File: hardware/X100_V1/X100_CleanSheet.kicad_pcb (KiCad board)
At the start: 4 copper layers, 45 x 45 mm, 205 parts, among them J401 124019772112A, J501 1040310811, J601 SM04B-GHS-TB(LF)(SN), J701 SM06B-GHS-TB(LF)(SN), J702 SM06B-GHS-TB(LF)(SN), J703 SM06B-GHS-TB(LF)(SN), J704 SM04B-GHS-TB(LF)(SN), J801 OUT1 /GND, J802 OUT2 /GND, J803 OUT3 /GND, J804 OUT4 /GND, J805 OUT5 /GND, J806 OUT6 /GND, J807 SWD:1REF2GND3IO4CLK5NRST, J808 BATTERY/bench3S-6S ONLY, J809 CURRENT monitor only, Q101 DMP6023LSS-13, U101 TPS54360BDDAR, U102 AP63203WU-7, U103 TPS7A2033PDBVR, U104 TPS2553DBVR, U201 STM32H743VIT6, U301 BMI088, U302 SPL06-001, U401 TPD2E2U06QDBZRQ1, U402 SN74LVC1G17DBVR, U403 TPD2E2U06QDBZRQ1, U404 TPD2E2U06QDBZRQ1, U601 TCAN3414DR, U801 TMUX1511PWR, Y201 8.000MHz /CL20pF

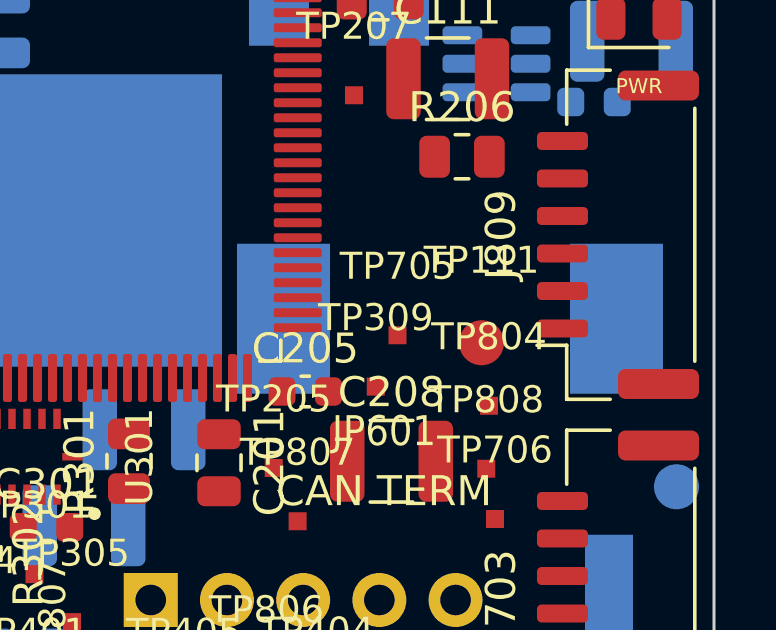
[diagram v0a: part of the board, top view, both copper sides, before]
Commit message: Adopt approved L101 SRP1038A and review actual 5V load
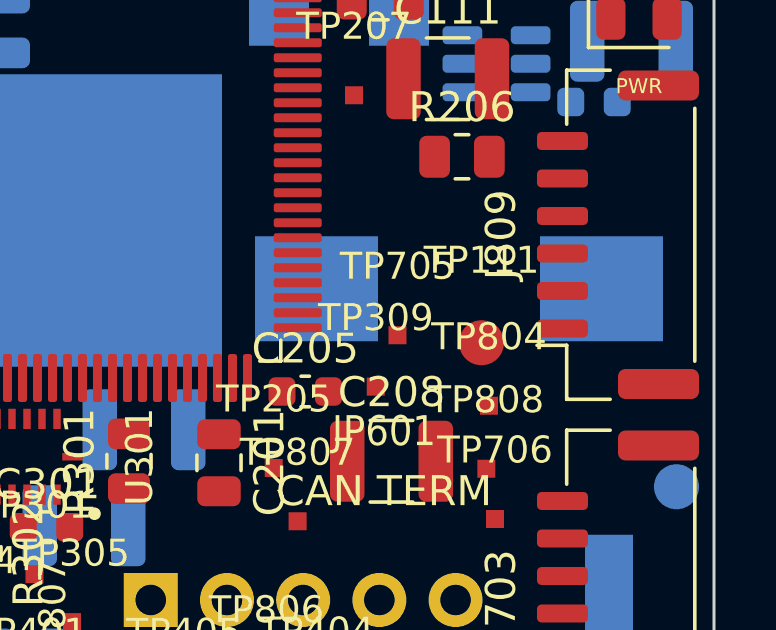
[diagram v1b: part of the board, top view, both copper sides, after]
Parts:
- L101: footprint X100_Physical:Bourns_SRP1265A -> X100_Physical:Bourns_SRP1038A_LeadFrame_NoVIP
- moved L101 1.04 mm to (114.0, 97.0)
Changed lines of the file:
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@@
 		)
 	)
-	(footprint "X100_Physical:Bourns_SRP1265A"
+	(footprint "X100_Physical:Bourns_SRP1038A_LeadFrame_NoVIP"
 		(layer "B.Cu")
-		(at 113.7 98)
-		(descr "Bourns SRP1265A official land 14.2/8.0/5.0mm")
+		(at 114 97)
+		(descr "Bourns SRP1038A-100M lead-frame; official layout outer13.6 gap5.4 height3.5 => pads4.1x3.5 centres9.5; maxcase11.5x10.3x4.0; no drill/noVIP; candidate only")
 		(property "Reference" "L101"
-			(at 0 8.25 180)
+			(at 0 6.5 180)
 			(layer "B.SilkS")
 			(effects
 				(font
-					(size 0.9 0.9)
+					(size 1 1)
+					(thickness 0.15)
 				)
 				(justify mirror)
@@
 		)
 		(property "Value" "10uH"
-			(at 0 -8.25 180)
+			(at 0 -6.5 180)
 			(layer "B.Fab")
 			(effects
 				(font
-					(size 0.9 0.9)
+					(size 1 1)
+					(thickness 0.15)
 				)
 				(justify mirror)
 			)
 		)
-		(property "Datasheet" "https://www.bourns.com/docs/product-datasheets/srp1265a.pdf"
+		(property "Datasheet" "https://www.bourns.com/docs/product-datasheets/srp1038a.pdf"
 			(at 0 0 180)
 			(layer "B.Fab")
-			(hide yes)
 			(effects
 				(font
-					(size 1.27 1.27)
+					(size 1 1)
+					(thickness 0.15)
 				)
 				(justify mirror)
 			)
 		)
-		(property "Description" ""
+		(property "Description" "Bourns SRP1038A-100M; lead-frame; max case11.5x10.3x4.0mm; user-approved20261023"
 			(at 0 0 180)
 			(layer "B.Fab")
@@
 		)
 		(property "Manufacturer" "Bourns"
-			(at 0 0 180)
-			(unlocked yes)
+			(at 0 0 0)
 			(layer "B.Fab")
 			(hide yes)
 			(effects
 				(font
-					(size 1 1)
+					(size 1.27 1.27)
 					(thickness 0.15)
 				)
-				(justify mirror)
 			)
 		)
-		(property "MPN" "SRP1265A-100M"
-			(at 0 0 180)
-			(unlocked yes)
+		(property "MPN" "SRP1038A-100M"
+			(at 0 0 0)
 			(layer "B.Fab")
 			(hide yes)
 			(effects
 				(font
-					(size 1 1)
+					(size 1.27 1.27)
 					(thickness 0.15)
 				)
-				(justify mirror)
 			)
 		)
-		(property "Package" "13.5x12.5x6.2 SMD"
-			(at 0 0 180)
-			(unlocked yes)
+		(property "Package" "Lead-frame SMD; case max11.5x10.3x4.0mm"
+			(at 0 0 0)
 			(layer "B.Fab")
 			(hide yes)
 			(effects
 				(font
-					(size 1 1)
+					(size 1.27 1.27)
 					(thickness 0.15)
 				)
-				(justify mirror)
 			)
 		)
-		(property "Procurement Policy" "EXACT_MPN_FROZEN"
-			(at 0 0 180)
-			(unlocked yes)
+		(property "Procurement Policy" "EXACT_MPN_FROZEN; USER_APPROVED_20261023; NO_PURCHASE"
+			(at 0 0 0)
 			(layer "B.Fab")
 			(hide yes)
 			(effects
 				(font
-					(size 1 1)
+					(size 1.27 1.27)
 					(thickness 0.15)
 				)
-				(justify mirror)
 			)
 		)
-		(property ki_fp_filters "Bourns_SRP1265A")
-		(sheetname "/01_POWER/")
-		(sheetfile "01_POWER.kicad_sch")
-		(units
-			(unit
-				(name "A")
-				(pins "1" "2")
+		(property "LCSC" "C780184"
+			(at 0 0 0)
+			(layer "B.Fab")
+			(hide yes)
+			(effects
+				(font
+					(size 1.27 1.27)
+					(thickness 0.15)
+				)
+			)
+		)
+		(property "Inductance" "10uH +/-20% @100kHz/1V"
+			(at 0 0 0)
+			(layer "B.Fab")
+			(hide yes)
+			(effects
+				(font
+					(size 1.27 1.27)
+					(thickness 0.15)
+				)
+			)
+		)
+		(property "DCR Max" "30mOhm @25C"
+			(at 0 0 0)
+			(layer "B.Fab")
+			(hide yes)
+			(effects
+				(font
+					(size 1.27 1.27)
+					(thickness 0.15)
+				)
+			)
+		)
+		(property "Irms" "7.5A; rated40C rise; application thermal test required"
+			(at 0 0 0)
+			(layer "B.Fab")
+			(hide yes)
+			(effects
+				(font
+					(size 1.27 1.27)
+					(thickness 0.15)
+				)
+			)
+		)
+		(property "Isat" "12A @25C for20% L drop; not hot minimum guarantee"
+			(at 0 0 0)
+			(layer "B.Fab")
+			(hide yes)
+			(effects
+				(font
+					(size 1.27 1.27)
+					(thickness 0.15)
+				)
+			)
+		)
+		(property "Verification Status" "DATASHEET_AND_LAYOUT_VERIFIED; POWER_REVIEW_OPEN; NO_BENCH_PASS"
+			(at 0 0 0)
+			(layer "B.Fab")
+			(hide yes)
+			(effects
+				(font
+					(size 1.27 1.27)
+					(thickness 0.15)
+				)
 			)
 		)
@@
 		(duplicate_pad_numbers_are_jumpers no)
 		(fp_rect
-			(start -7.6 6.75)
-			(end 7.6 -6.75)
+			(start -7.3 5.65)
+			(end 7.3 -5.65)
 			(stroke
 				(width 0.05)
@@
 		)
 		(fp_rect
-			(start -6.75 6.25)
-			(end 6.75 -6.25)
+			(start -5.75 5.15)
+			(end 5.75 -5.15)
 			(stroke
 				(width 0.1)
@@
 		)
 		(pad "1" smd rect
-			(at -5.55 0)
-			(size 3.1 5)
+			(at -4.75 0)
+			(size 4.1 3.5)
 			(layers "B.Cu" "B.Mask" "B.Paste")
 			(net "MAIN_SW")
-			(pinfunction "1_1")
-			(pintype "passive")
 		)
 		(pad "2" smd rect
-			(at 5.55 0)
-			(size 3.1 5)
+			(at 4.75 0)
+			(size 4.1 3.5)
 			(layers "B.Cu" "B.Mask" "B.Paste")
 			(net "5V_MAIN")
-			(pinfunction "2_2")
-			(pintype "passive")
 		)
 		(embedded_fonts no)
